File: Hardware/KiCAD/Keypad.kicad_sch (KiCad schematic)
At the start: 1 part, among them IC9 PCF8575PWR

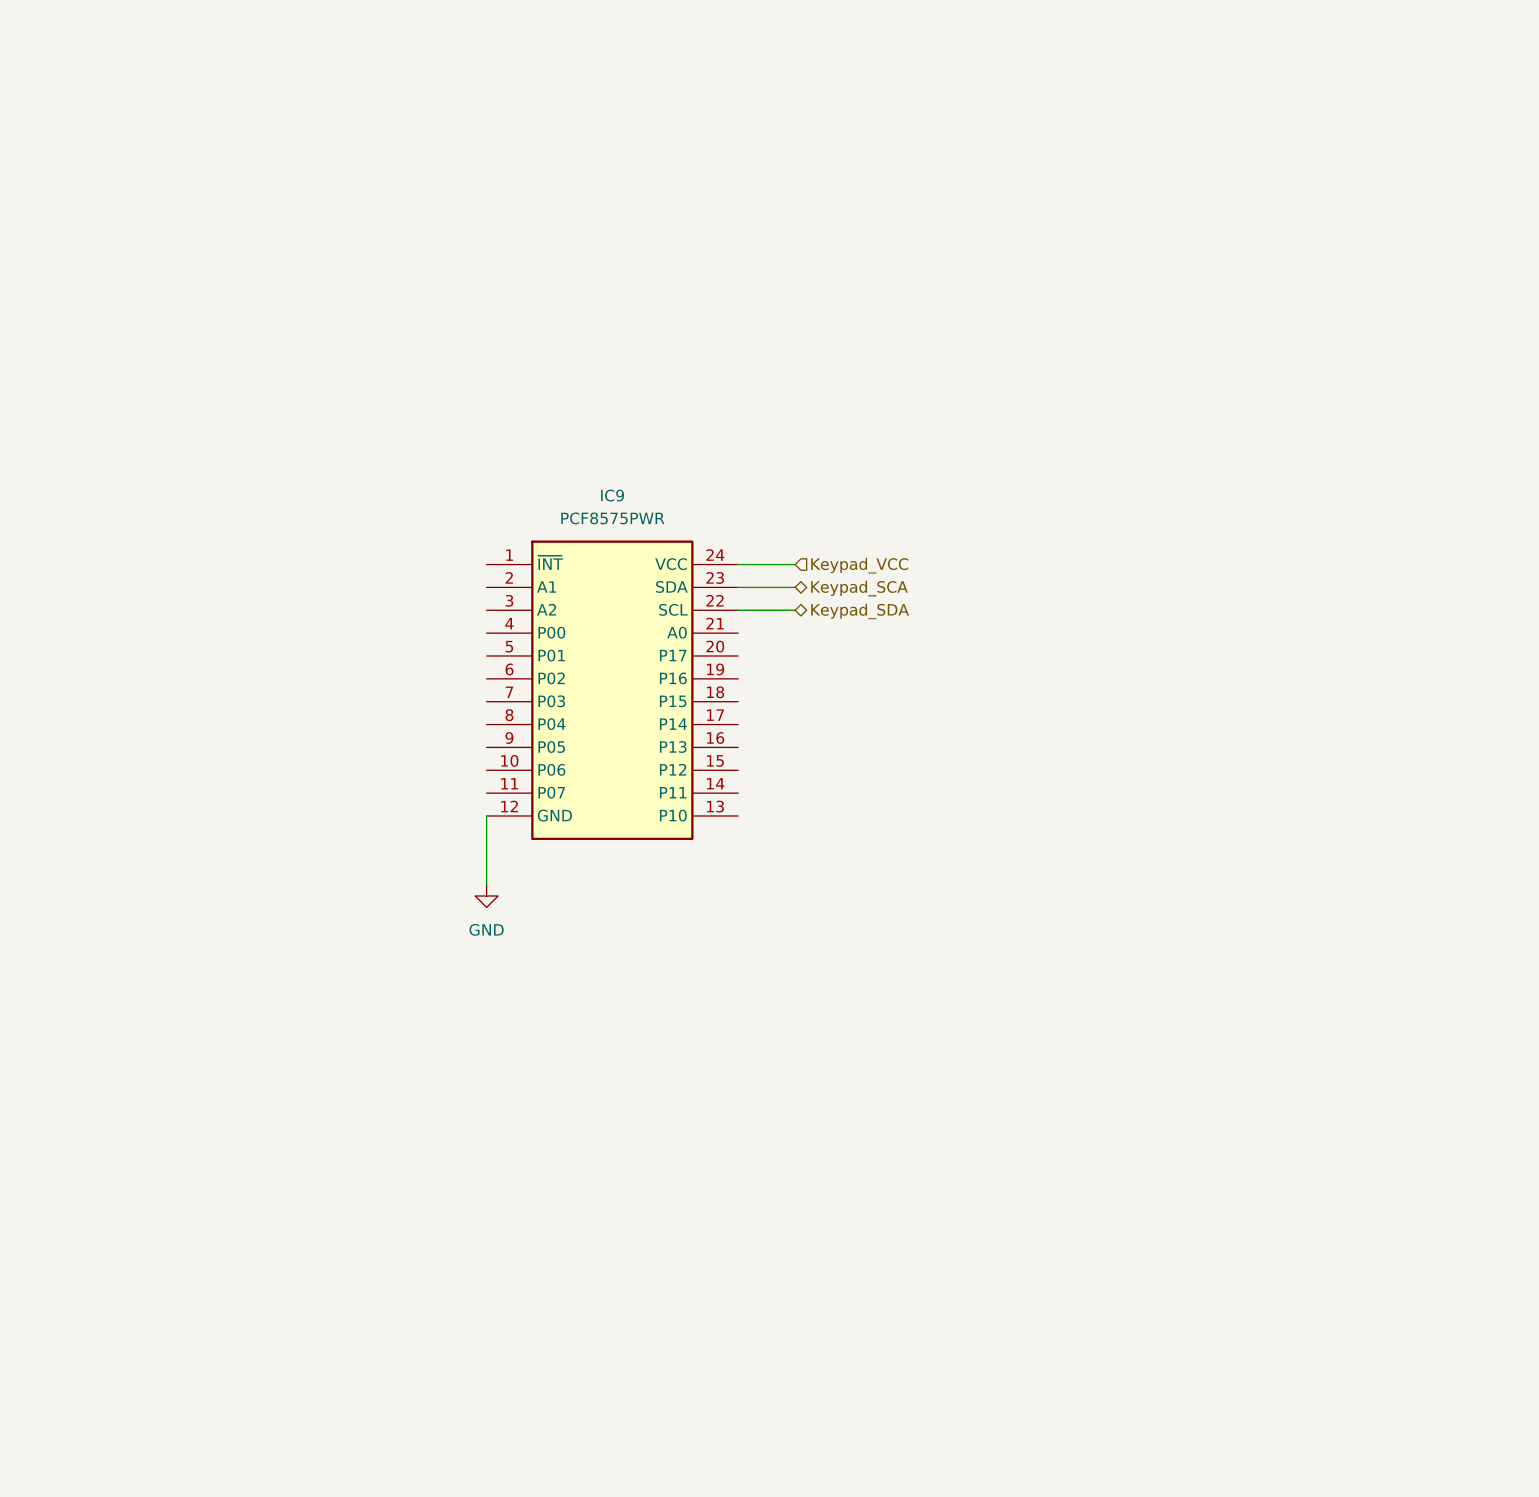
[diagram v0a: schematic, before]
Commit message: Changed Keypad to better accomidate use of GPIO and removed inc symbols
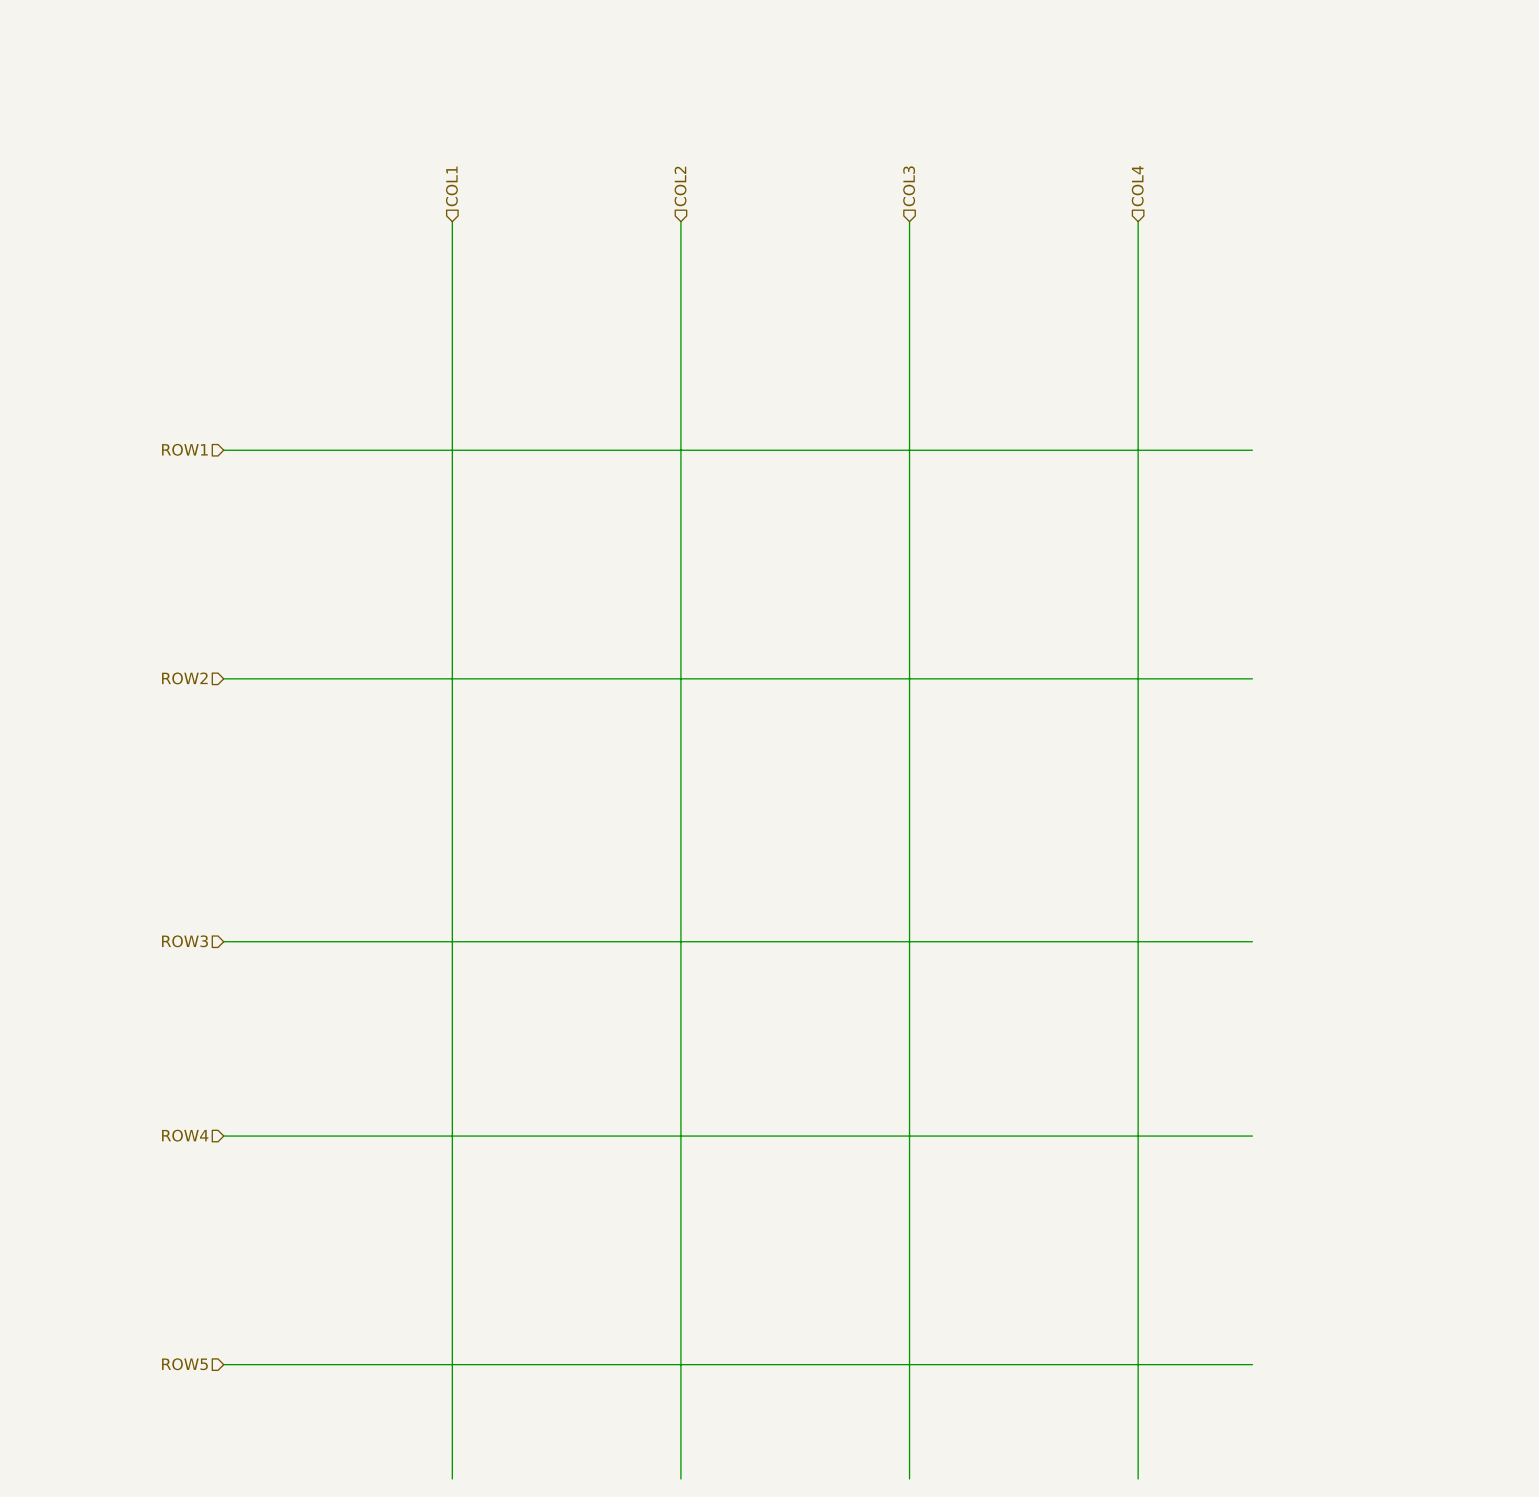
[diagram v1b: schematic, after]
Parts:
- removed IC9: PCF8575PWR, Cobalt_Cowboy:SOP65P640X120-24N_PCF8575PWR, symbol Cobalt-Cowboy:PCF8575PWR
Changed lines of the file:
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@@
 (kicad_sch (version 20230121) (generator eeschema)
   (paper "A4")
-  (wire (pts (xy 67.31 104.14) (xy 67.31 111.76))
+  (wire (pts (xy 38.1 118.11) (xy 152.4 118.11))
     (stroke (width 0) (type default))
   )
-  (wire (pts (xy 95.25 78.74) (xy 101.6 78.74))
+  (wire (pts (xy 38.1 63.5) (xy 152.4 63.5))
     (stroke (width 0) (type default))
   )
-  (wire (pts (xy 95.25 76.2) (xy 101.6 76.2))
+  (wire (pts (xy 63.5 38.1) (xy 63.5 177.8))
     (stroke (width 0) (type default))
   )
-  (wire (pts (xy 95.25 81.28) (xy 101.6 81.28))
+  (wire (pts (xy 88.9 38.1) (xy 88.9 177.8))
     (stroke (width 0) (type default))
   )
-  (hierarchical_label "Keypad_SCA" (shape bidirectional) (at 101.6 78.74 0) (fields_autoplaced)
+  (wire (pts (xy 38.1 88.9) (xy 152.4 88.9))
+    (stroke (width 0) (type default))
+  )
+  (wire (pts (xy 114.3 38.1) (xy 114.3 177.8))
+    (stroke (width 0) (type default))
+  )
+  (wire (pts (xy 139.7 38.1) (xy 139.7 177.8))
+    (stroke (width 0) (type default))
+  )
+  (wire (pts (xy 38.1 139.7) (xy 152.4 139.7))
+    (stroke (width 0) (type default))
+  )
+  (wire (pts (xy 38.1 165.1) (xy 152.4 165.1))
+    (stroke (width 0) (type default))
+  )
+  (hierarchical_label "ROW2" (shape input) (at 38.1 88.9 180) (fields_autoplaced)
+    (effects (font (size 1.27 1.27)) (justify right))
+  )
+  (hierarchical_label "ROW4" (shape input) (at 38.1 139.7 180) (fields_autoplaced)
+    (effects (font (size 1.27 1.27)) (justify right))
+  )
+  (hierarchical_label "COL2" (shape input) (at 88.9 38.1 90) (fields_autoplaced)
     (effects (font (size 1.27 1.27)) (justify left))
   )
-  (hierarchical_label "Keypad_SDA" (shape bidirectional) (at 101.6 81.28 0) (fields_autoplaced)
+  (hierarchical_label "COL4" (shape input) (at 139.7 38.1 90) (fields_autoplaced)
     (effects (font (size 1.27 1.27)) (justify left))
   )
-  (hierarchical_label "Keypad_VCC" (shape input) (at 101.6 76.2 0) (fields_autoplaced)
+  (hierarchical_label "COL3" (shape input) (at 114.3 38.1 90) (fields_autoplaced)
     (effects (font (size 1.27 1.27)) (justify left))
   )
-  (symbol (lib_id "Cobalt-Cowboy:PCF8575PWR") (at 67.31 76.2 0) (unit 1)
-    (in_bom yes) (on_board yes) (dnp no) (fields_autoplaced)
-    (property "Reference" "IC9" (at 81.28 68.58 0)
-      (effects (font (size 1.27 1.27)))
-    )
-    (property "Value" "PCF8575PWR" (at 81.28 71.12 0)
-      (effects (font (size 1.27 1.27)))
-    )
-    (property "Footprint" "Cobalt_Cowboy:SOP65P640X120-24N_PCF8575PWR" (at 91.44 171.12 0)
-      (effects (font (size 1.27 1.27)) (justify left top) hide)
-    )
-    (property "Datasheet" "http://www.ti.com/lit/gpn/pcf8575" (at 91.44 271.12 0)
-      (effects (font (size 1.27 1.27)) (justify left top) hide)
-    )
-    (property "Height" "1.2" (at 91.44 471.12 0)
-      (effects (font (size 1.27 1.27)) (justify left top) hide)
-    )
-    (property "Manufacturer_Name" "Texas Instruments" (at 91.44 571.12 0)
-      (effects (font (size 1.27 1.27)) (justify left top) hide)
-    )
-    (property "Manufacturer_Part_Number" "PCF8575PWR" (at 91.44 671.12 0)
-      (effects (font (size 1.27 1.27)) (justify left top) hide)
-    )
-    (property "Mouser Part Number" "595-PCF8575PWR" (at 91.44 771.12 0)
-      (effects (font (size 1.27 1.27)) (justify left top) hide)
-    )
-    (property "Mouser Price/Stock" "https://www.mouser.co.uk/ProductDetail/Texas-Instruments/PCF8575PWR?qs=wgAEGBTxy7lfNLEoaenBaA%3D%3D" (at 91.44 871.12 0)
-      (effects (font (size 1.27 1.27)) (justify left top) hide)
-    )
-    (property "Arrow Part Number" "PCF8575PWR" (at 91.44 971.12 0)
-      (effects (font (size 1.27 1.27)) (justify left top) hide)
-    )
-    (property "Arrow Price/Stock" "https://www.arrow.com/en/products/pcf8575pwr/texas-instruments?region=nac" (at 91.44 1071.12 0)
-      (effects (font (size 1.27 1.27)) (justify left top) hide)
-    )
-    (pin "11")
-    (pin "12")
-    (pin "19")
-    (pin "20")
-    (pin "24")
-    (pin "14")
-    (pin "13")
-    (pin "15")
-    (pin "10")
-    (pin "1")
-    (pin "16")
-    (pin "9")
-    (pin "17")
-    (pin "23")
-    (pin "2")
-    (pin "5")
-    (pin "4")
-    (pin "18")
-    (pin "3")
-    (pin "22")
-    (pin "8")
-    (pin "21")
-    (pin "7")
-    (pin "6")
-    (instances
-      (project "Cobalt-Cowboy"
-        (path "/60a68eb1-aa0f-414e-b03b-965ad6b52dab/1039084b-a0e1-47ac-823b-a237cfc3ed39/36b248bc-2a23-4171-b336-2df6d7e58962"
-          (reference "IC9") (unit 1)
-        )
-      )
-    )
+  (hierarchical_label "ROW3" (shape input) (at 38.1 118.11 180) (fields_autoplaced)
+    (effects (font (size 1.27 1.27)) (justify right))
   )
-  (symbol (lib_id "power:GND") (at 67.31 111.76 0) (unit 1)
-    (in_bom yes) (on_board yes) (dnp no) (fields_autoplaced)
-    (property "Reference" "#PWR03" (at 67.31 118.11 0)
-      (effects (font (size 1.27 1.27)) hide)
-    )
-    (property "Value" "GND" (at 67.31 116.84 0)
-      (effects (font (size 1.27 1.27)))
-    )
-    (property "Footprint" "" (at 67.31 111.76 0)
-      (effects (font (size 1.27 1.27)) hide)
-    )
-    (property "Datasheet" "" (at 67.31 111.76 0)
-      (effects (font (size 1.27 1.27)) hide)
-    )
-    (pin "1")
-    (instances
-      (project "Cobalt-Cowboy"
-        (path "/60a68eb1-aa0f-414e-b03b-965ad6b52dab/1039084b-a0e1-47ac-823b-a237cfc3ed39/36b248bc-2a23-4171-b336-2df6d7e58962"
-          (reference "#PWR03") (unit 1)
-        )
-      )
-    )
+  (hierarchical_label "ROW5" (shape input) (at 38.1 165.1 180) (fields_autoplaced)
+    (effects (font (size 1.27 1.27)) (justify right))
+  )
+  (hierarchical_label "COL1" (shape input) (at 63.5 38.1 90) (fields_autoplaced)
+    (effects (font (size 1.27 1.27)) (justify left))
+  )
+  (hierarchical_label "ROW1" (shape input) (at 38.1 63.5 180) (fields_autoplaced)
+    (effects (font (size 1.27 1.27)) (justify right))
   )
 )

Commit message: Added seperate schematic for amplifier assembly
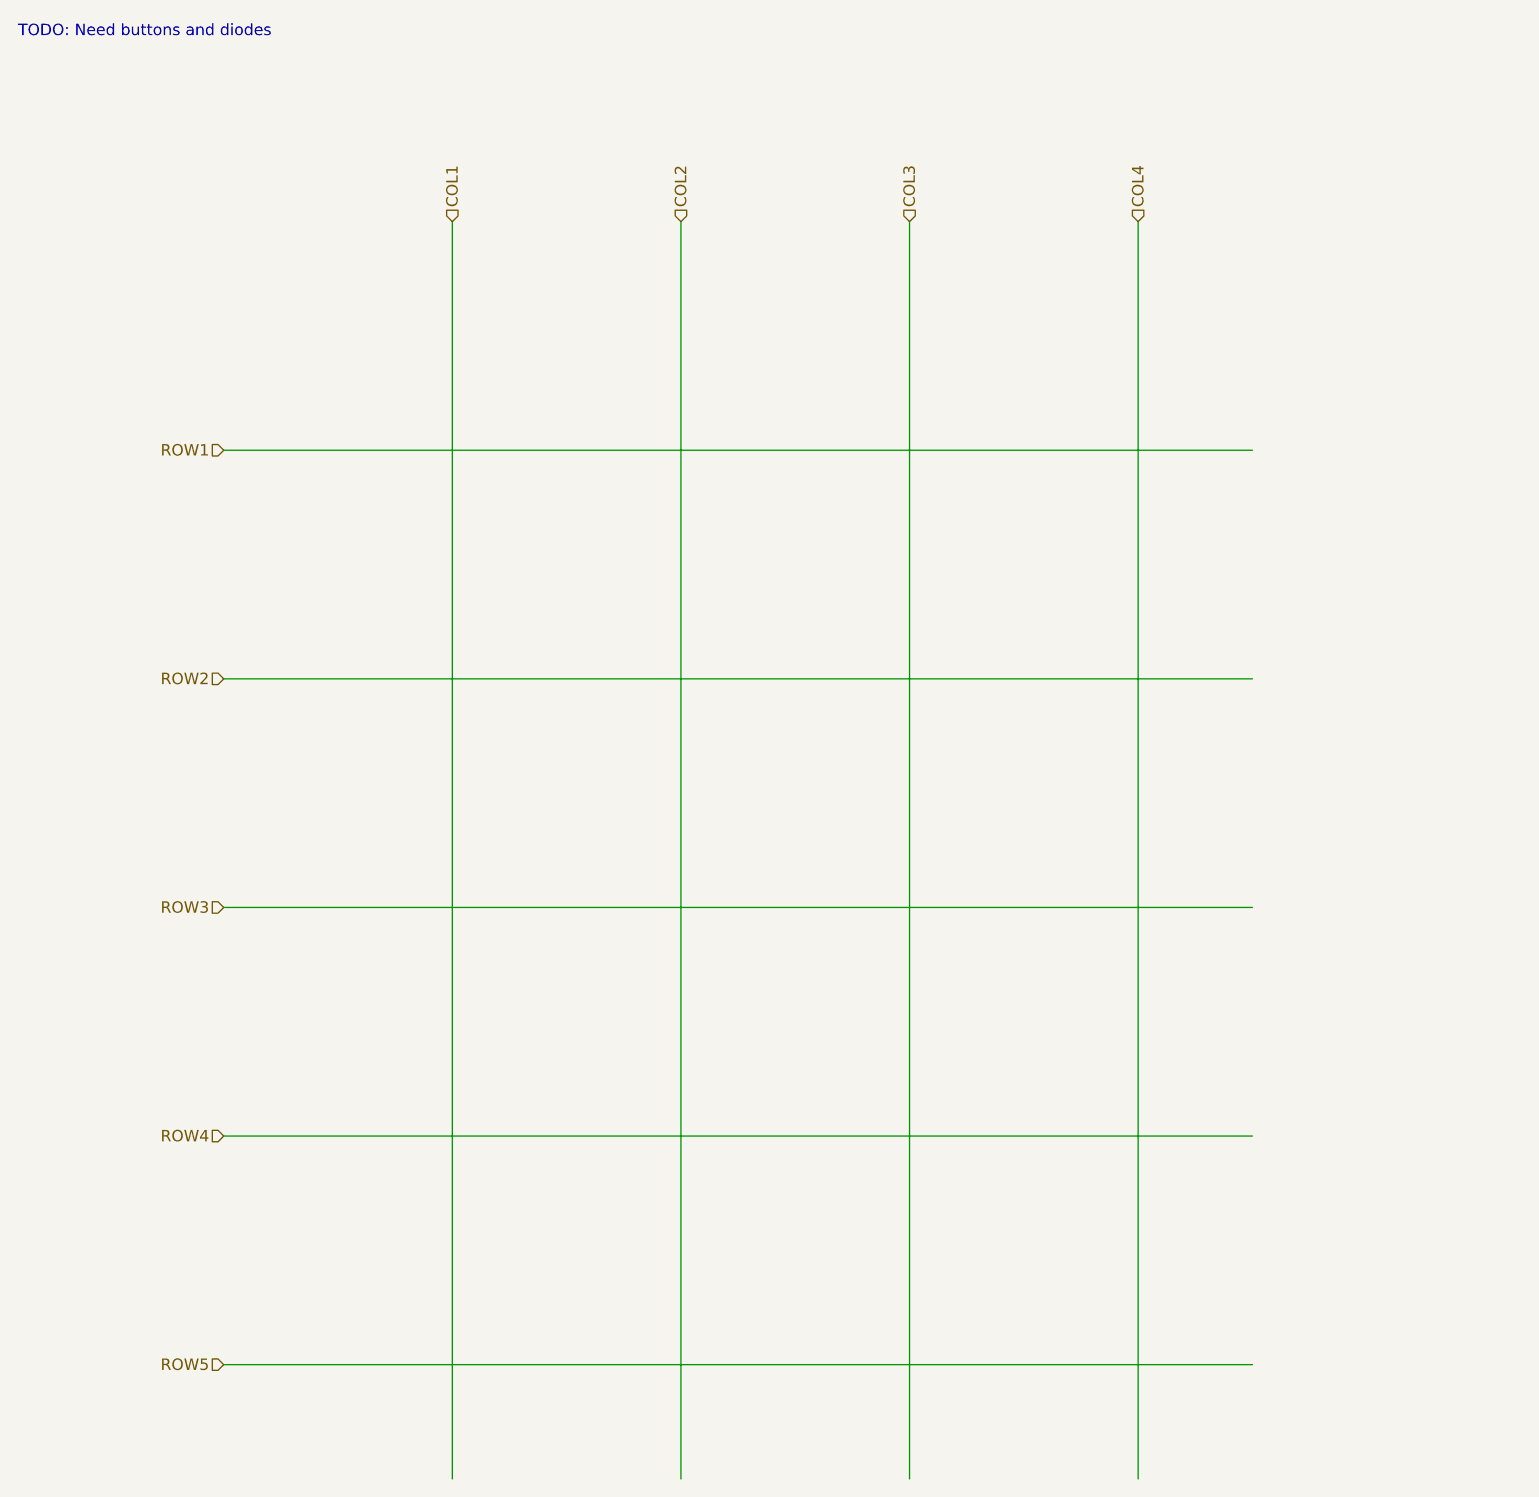
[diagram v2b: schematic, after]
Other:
- note added: "TODO: Need buttons and diodes"
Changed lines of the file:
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@@
 (kicad_sch (version 20230121) (generator eeschema)
   (paper "A4")
-  (wire (pts (xy 38.1 118.11) (xy 152.4 118.11))
+  (wire (pts (xy 38.1 114.3) (xy 152.4 114.3))
     (stroke (width 0) (type default))
   )
@@
     (stroke (width 0) (type default))
   )
+  (text "TODO: Need buttons and diodes\n" (at 15.24 17.78 0)
+    (effects (font (size 1.27 1.27)) (justify left bottom))
+  )
   (hierarchical_label "ROW2" (shape input) (at 38.1 88.9 180) (fields_autoplaced)
     (effects (font (size 1.27 1.27)) (justify right))
@@
     (effects (font (size 1.27 1.27)) (justify left))
   )
-  (hierarchical_label "ROW3" (shape input) (at 38.1 118.11 180) (fields_autoplaced)
+  (hierarchical_label "ROW3" (shape input) (at 38.1 114.3 180) (fields_autoplaced)
     (effects (font (size 1.27 1.27)) (justify right))
   )
